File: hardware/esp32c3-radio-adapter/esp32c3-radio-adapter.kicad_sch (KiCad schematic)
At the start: 12 parts, among them J1 Conn_01x08, J2 Conn_01x08, J3 E07-M1101D_or_Ra-02, J4 Expansion

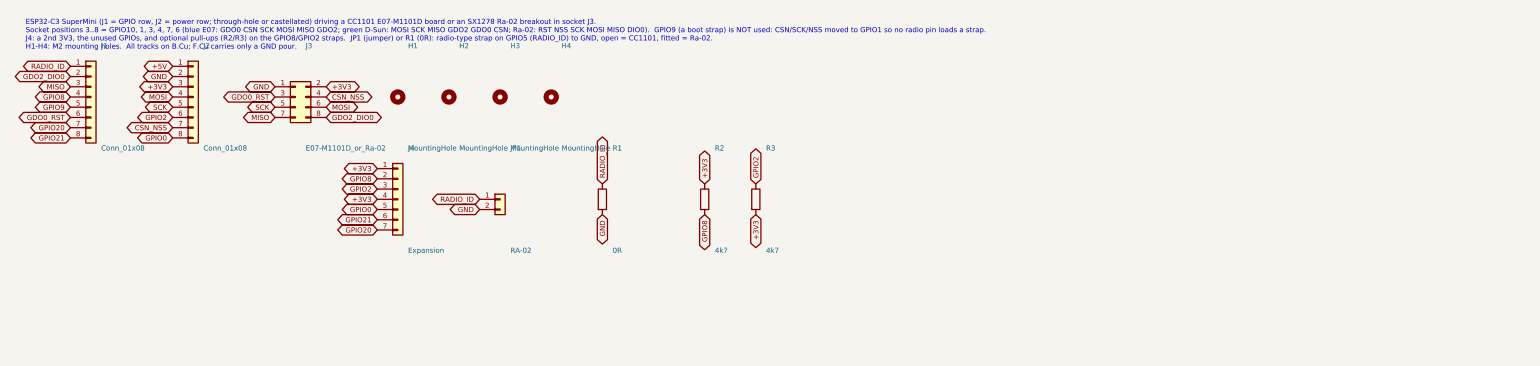
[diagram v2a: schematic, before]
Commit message: Socket adapter: J5, a fly-wire header for the SX1278's DIO2/DATA pin
In the SX1278's continuous mode the raw bitstream reaches the outside
world only on DIO2/DATA -- the FIFO and packet handler are inactive, and
Table 29 gives no other DIO that can carry it in Rx.  Packet mode can't
stand in: it only carries what the chip's packet handler can frame, which
is fine for the Fineoffset stations but useless for the OOK remotes this
node exists to hear and key.  DIO2 is the SX1278's GDO2, and the Ra-02
breakout leaves it on the module edge, unconnected.

Add J5, a 1x2 header carrying GPIO21 and GPIO20, so one wire from an
Ra-02's DIO2 pad reaches a GPIO.  GPIO20 is that pin; both stay on J4 as
well, so nothing is lost -- one net, brought out twice.

Placing it took the board from 36.5 to 38.0 mm tall.  A 2.54 mm header
body and both plugged-in boards all sit at board level, so the header has
to be clear of them in plan view, and the only such region is the band
between the SuperMini's body and the radio board's top edge.  At 36.5 mm
that band is 4.08 mm, which leaves 0.79 mm either side of the body;
1.5 mm more opens it to 5.58 mm and takes both margins to 1.54 mm.

Routing stays single-sided.  GPIO21 drops right of GPIO20, so it must
take the lane above J5's pads (25.29) and stubs down into pin 1; GPIO20
takes the lane below (27.8) and climbs the strip straight through its own
pad, pin 2.  That fixes which net is on which pin: GPIO20's strip lane
has to pass through a pad of its own net, and the gap right of pin 2 is
only 0.235 mm.  The four strip lanes shift left 0.45 mm to make room
(GPIO21 22.9, GPIO20 23.35) and 3V3/GND move out to 24.55/25.0, still
0.375 mm clear of the M2 holes.

GND is not on J5: reaching it would mean crossing the 3V3 strip lane, and
it isn't needed -- the boards already share GND through the socket.

The SX1278 module adapter is untouched; its pin allocation is to be
brought into line with this board separately.

Co-Authored-By: Claude Opus 5 (1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
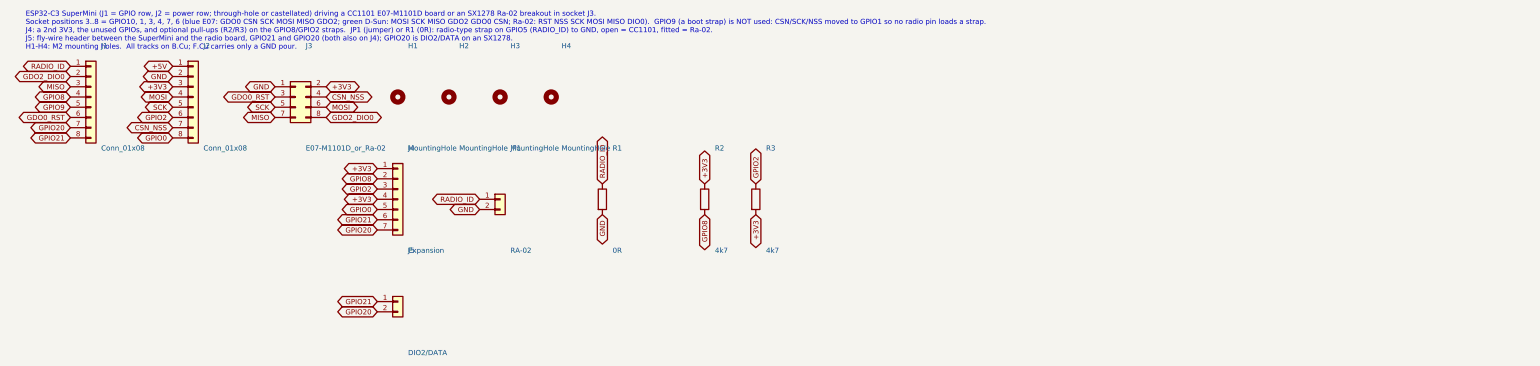
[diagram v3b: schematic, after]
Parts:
- added J5: DIO2/DATA, Adapter:PinHeader_1x02_P2.54mm_Vertical, symbol Connector_Generic:Conn_01x02
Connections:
- net GPIO20: now also J5.2 (Pin_2)
- net GPIO21: now also J5.1 (Pin_1)
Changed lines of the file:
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@@
+	)
+	(symbol
+		(lib_id "Connector_Generic:Conn_01x02")
+		(at 152.4 152.4 0)
+		(unit 1)
+		(exclude_from_sim no)
+		(in_bom yes)
+		(on_board yes)
+		(dnp no)
+		(fields_autoplaced yes)
+		(property "Reference" "J5"
+			(at 154.94 139.7 0)
+			(effects
+				(font
+					(size 1.27 1.27)
+				)
+				(justify left)
+			)
+		)
+		(property "Value" "DIO2/DATA"
+			(at 154.94 165.1 0)
+			(effects
+				(font
+					(size 1.27 1.27)
+				)
+				(justify left)
+			)
+		)
+		(property "Footprint" "Adapter:PinHeader_1x02_P2.54mm_Vertical"
+			(at 152.4 152.4 0)
+			(effects
+				(font
+					(size 1.27 1.27)
+				)
+				(hide yes)
+			)
+		)
+		(property "Datasheet" "~"
+			(at 152.4 152.4 0)
+			(effects
+				(font
+					(size 1.27 1.27)
+				)
+				(hide yes)
+			)
+		)
+		(property "Description" "Fly-wire header beside the socket: pin 2 (GPIO20) is the SX1278's DIO2/DATA raw-bitstream pin, pin 1 (GPIO21) a spare"
+			(at 152.4 152.4 0)
+			(effects
+				(font
+					(size 1.27 1.27)
+				)
+				(hide yes)
+			)
+		)
+		(pin "1"
+		)
+		(pin "2"
+		)
+		(instances
+			(project "esp32c3-radio-adapter"
+				(path "/b71943b6-a88f-5429-bfd6-fb1a52f93b27"
+					(reference "J5")
+					(unit 1)
+				)
+			)
+		)
+	)
+	(global_label "GPIO21"
+		(shape bidirectional)
+		(at 147.32 152.4 180)
+		(fields_autoplaced yes)
+		(effects
+			(font
+				(size 1.27 1.27)
+			)
+			(justify right)
+		)
+		(property "Intersheetrefs" "${INTERSHEET_REFS}"
+			(at 147.32 152.4 0)
+			(effects
+				(font
+					(size 1.27 1.27)
+				)
+				(justify right)
+				(hide yes)
+			)
+		)
+	)
+	(global_label "GPIO20"
+		(shape bidirectional)
+		(at 147.32 154.94 180)
+		(fields_autoplaced yes)
+		(effects
+			(font
+				(size 1.27 1.27)
+			)
+			(justify right)
+		)
+		(property "Intersheetrefs" "${INTERSHEET_REFS}"
+			(at 147.32 154.94 0)
+			(effects
+				(font
+					(size 1.27 1.27)
+				)
+				(justify right)
+				(hide yes)
+			)
+		)
 	)
 	(symbol
@@
 		)
 	)
-	(text "ESP32-C3 SuperMini (J1 = GPIO row, J2 = power row; through-hole or castellated) driving a CC1101 E07-M1101D board or an SX1278 Ra-02 breakout in socket J3.\nSocket positions 3..8 = GPIO10, 1, 3, 4, 7, 6 (blue E07: GDO0 CSN SCK MOSI MISO GDO2; green D-Sun: MOSI SCK MISO GDO2 GDO0 CSN; Ra-02: RST NSS SCK MOSI MISO DIO0).  GPIO9 (a boot strap) is NOT used: CSN/SCK/NSS moved to GPIO1 so no radio pin loads a strap.\nJ4: a 2nd 3V3, the unused GPIOs, and optional pull-ups (R2/R3) on the GPIO8/GPIO2 straps.  JP1 (jumper) or R1 (0R): radio-type strap on GPIO5 (RADIO_ID) to GND, open = CC1101, fitted = Ra-02.\nH1-H4: M2 mounting holes.  All tracks on B.Cu; F.Cu carries only a GND pour."
+	(text "ESP32-C3 SuperMini (J1 = GPIO row, J2 = power row; through-hole or castellated) driving a CC1101 E07-M1101D board or an SX1278 Ra-02 breakout in socket J3.\nSocket positions 3..8 = GPIO10, 1, 3, 4, 7, 6 (blue E07: GDO0 CSN SCK MOSI MISO GDO2; green D-Sun: MOSI SCK MISO GDO2 GDO0 CSN; Ra-02: RST NSS SCK MOSI MISO DIO0).  GPIO9 (a boot strap) is NOT used: CSN/SCK/NSS moved to GPIO1 so no radio pin loads a strap.\nJ4: a 2nd 3V3, the unused GPIOs, and optional pull-ups (R2/R3) on the GPIO8/GPIO2 straps.  JP1 (jumper) or R1 (0R): radio-type strap on GPIO5 (RADIO_ID) to GND, open = CC1101, fitted = Ra-02.\nJ5: fly-wire header between the SuperMini and the radio board, GPIO21 and GPIO20 (both also on J4); GPIO20 is DIO2/DATA on an SX1278.\nH1-H4: M2 mounting holes.  All tracks on B.Cu; F.Cu carries only a GND pour."
 		(exclude_from_sim no)
 		(at 60 90 0)

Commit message: Socket adapter: R4, a GPIO9 pull-up footprint, and clearer silkscreen
GPIO9 is the boot strap the socket no longer carries.  Give it the same
optional do-not-populate 4k7 pull-up to 3V3 the other two straps have.
Its pad is boxed in on the back copper (SCK passes left of it and drops
into the socket pin directly beneath, CSN passes right of it), so:
SCK steps one gap left as soon as it leaves its pad, J4 pins 3 and 4
swap so the second 3V3 sits left of GPIO2 like the first sits left of
GPIO8, and that 3V3 pin feeds down through the power row's GPIO3/GPIO2
gap into R4, whose other pad drops into GPIO9.  CSN keeps right of R4
until it is above the GPIO row's rings.  Still every track on B.Cu; DRC
clean.

Silkscreen: every SuperMini pin now has an inner label (NC, GND, 3V3,
J4, J4/J5, R4, JP1, DIO2 for the pins that carried none); the USB-C is
drawn as its outline instead of a word, solid on the front and dashed
on the back; every outline on the back is dashed; the "all tracks"
notes go, replaced by "parts this side" on the front.  Under the USB-C
outline the two columns' labels are shortened or split into two lines.

Co-Authored-By: Claude Opus 5 (1M context) <noreply@anthropic.com>
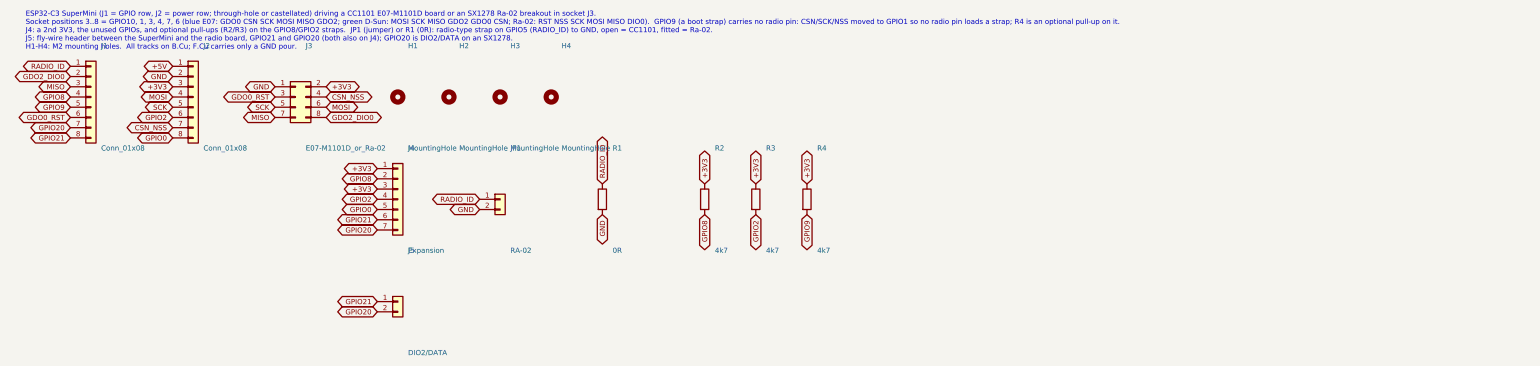
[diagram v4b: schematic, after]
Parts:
- added R4: 4k7, Adapter:R_0805_2012Metric_HandSolder_AlongY_Back, symbol Device:R
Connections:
- net +3V3: now also J4.3 (Pin_3), R3.1, R4.1; no longer J4.4 (Pin_4), R3.2
- net GPIO2: now also J4.4 (Pin_4), R3.2; no longer J4.3 (Pin_3), R3.1
- net GPIO9: now also R4.2
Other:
- note added: "ESP32-C3 SuperMini (J1 = GPIO row, J2 = power row; through-hole or castellated) driving a CC1101 E07-M1101D board or an SX1278 Ra-02 breakout in socket J3. Socket positions 3..8 = GPIO10, 1, 3, 4, 7, 6 (blue E07: GDO0 CSN SCK MOSI MISO GDO2; green D-Sun: MOSI SCK MISO GDO2 GDO0 CSN; Ra-02: RST NSS SCK MOSI MISO DIO0). GPIO9 (a boot strap) carries no radio pin: CSN/SCK/NSS moved to GPIO1 so no rad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"
- note removed: "ESP32-C3 SuperMini (J1 = GPIO row, J2 = power row; through-hole or castellated) driving a CC1101 E07-M1101D board or an SX1278 Ra-02 breakout in socket J3. Socket positions 3..8 = GPIO10, 1, 3, 4, 7, 6 (blue E07: GDO0 CSN SCK MOSI MISO GDO2; green D-Sun: MOSI SCK MISO GDO2 GDO0 CSN; Ra-02: RST NSS SCK MOSI MISO DIO0). GPIO9 (a boot strap) is NOT used: CSN/SCK/NSS moved to GPIO1 so no radio pin lo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"
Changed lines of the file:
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@@
+		)
+	)
+	(global_label "+3V3"
+		(shape bidirectional)
+		(at 147.32 124.46 180)
+		(fields_autoplaced yes)
+		(effects
+			(font
+				(size 1.27 1.27)
+			)
+			(justify right)
+		)
+		(property "Intersheetrefs" "${INTERSHEET_REFS}"
+			(at 147.32 124.46 0)
+			(effects
+				(font
+					(size 1.27 1.27)
+				)
+				(justify right)
+				(hide yes)
+			)
 		)
 	)
 	(global_label "GPIO2"
-		(shape bidirectional)
-		(at 147.32 124.46 180)
-		(fields_autoplaced yes)
-		(effects
-			(font
-				(size 1.27 1.27)
-			)
-			(justify right)
-		)
-		(property "Intersheetrefs" "${INTERSHEET_REFS}"
-			(at 147.32 124.46 0)
-			(effects
-				(font
-					(size 1.27 1.27)
-				)
-				(justify right)
-				(hide yes)
-			)
-		)
-	)
-	(global_label "+3V3"
 		(shape bidirectional)
 		(at 147.32 127 180)
@@
 		)
 	)
+	(global_label "+3V3"
+		(shape bidirectional)
+		(at 241.3 123.19 90)
+		(fields_autoplaced yes)
+		(effects
+			(font
+				(size 1.27 1.27)
+			)
+			(justify left)
+		)
+		(property "Intersheetrefs" "${INTERSHEET_REFS}"
+			(at 241.3 123.19 0)
+			(effects
+				(font
+					(size 1.27 1.27)
+				)
+				(justify left)
+				(hide yes)
+			)
+		)
+	)
 	(global_label "GPIO2"
 		(shape bidirectional)
-		(at 241.3 123.19 90)
+		(at 241.3 130.81 270)
+		(fields_autoplaced yes)
+		(effects
+			(font
+				(size 1.27 1.27)
+			)
+			(justify right)
+		)
+		(property "Intersheetrefs" "${INTERSHEET_REFS}"
+			(at 241.3 130.81 0)
+			(effects
+				(font
+					(size 1.27 1.27)
+				)
+				(justify right)
+				(hide yes)
+			)
+		)
+	)
+	(symbol
+		(lib_id "Device:R")
+		(at 254 127 0)
+		(unit 1)
+		(exclude_from_sim no)
+		(in_bom yes)
+		(on_board yes)
+		(dnp no)
+		(fields_autoplaced yes)
+		(property "Reference" "R4"
+			(at 256.54 114.3 0)
+			(effects
+				(font
+					(size 1.27 1.27)
+				)
+				(justify left)
+			)
+		)
+		(property "Value" "4k7"
+			(at 256.54 139.7 0)
+			(effects
+				(font
+					(size 1.27 1.27)
+				)
+				(justify left)
+			)
+		)
+		(property "Footprint" "Adapter:R_0805_2012Metric_HandSolder_AlongY_Back"
+			(at 254 127 0)
+			(effects
+				(font
+					(size 1.27 1.27)
+				)
+				(hide yes)
+			)
+		)
+		(property "Datasheet" "~"
+			(at 254 127 0)
+			(effects
+				(font
+					(size 1.27 1.27)
+				)
+				(hide yes)
+			)
+		)
+		(property "Description" "Optional pull-up: GPIO9 boot strap to 3V3 (DNP unless needed)"
+			(at 254 127 0)
+			(effects
+				(font
+					(size 1.27 1.27)
+				)
+				(hide yes)
+			)
+		)
+		(pin "1"
+		)
+		(pin "2"
+		)
+		(instances
+			(project "esp32c3-radio-adapter"
+				(path "/b71943b6-a88f-5429-bfd6-fb1a52f93b27"
+					(reference "R4")
+					(unit 1)
+				)
+			)
+		)
+	)
+	(global_label "+3V3"
+		(shape bidirectional)
+		(at 254 123.19 90)
 		(fields_autoplaced yes)
 		(effects
@@
 		)
 		(property "Intersheetrefs" "${INTERSHEET_REFS}"
-			(at 241.3 123.19 0)
-			(effects
-				(font
-					(size 1.27 1.27)
-				)
-				(justify left)
-				(hide yes)
-			)
-		)
-	)
-	(global_label "+3V3"
-		(shape bidirectional)
-		(at 241.3 130.81 270)
-		(fields_autoplaced yes)
-		(effects
-			(font
-				(size 1.27 1.27)
-			)
-			(justify right)
-		)
-		(property "Intersheetrefs" "${INTERSHEET_REFS}"
-			(at 241.3 130.81 0)
+			(at 254 123.19 0)
+			(effects
+				(font
+					(size 1.27 1.27)
+				)
+				(justify left)
+				(hide yes)
+			)
+		)
+	)
+	(global_label "GPIO9"
+		(shape bidirectional)
+		(at 254 130.81 270)
+		(fields_autoplaced yes)
+		(effects
+			(font
+				(size 1.27 1.27)
+			)
+			(justify right)
+		)
+		(property "Intersheetrefs" "${INTERSHEET_REFS}"
+			(at 254 130.81 0)
 			(effects
 				(font
@@
 		)
 	)
-	(text "ESP32-C3 SuperMini (J1 = GPIO row, J2 = power row; through-hole or castellated) driving a CC1101 E07-M1101D board or an SX1278 Ra-02 breakout in socket J3.\nSocket positions 3..8 = GPIO10, 1, 3, 4, 7, 6 (blue E07: GDO0 CSN SCK MOSI MISO GDO2; green D-Sun: MOSI SCK MISO GDO2 GDO0 CSN; Ra-02: RST NSS SCK MOSI MISO DIO0).  GPIO9 (a boot strap) is NOT used: CSN/SCK/NSS moved to GPIO1 so no radio pin loads a strap.\nJ4: a 2nd 3V3, the unused GPIOs, and optional pull-ups (R2/R3) on the GPIO8/GPIO2 straps.  JP1 (jumper) or R1 (0R): radio-type strap on GPIO5 (RADIO_ID) to GND, open = CC1101, fitted = Ra-02.\nJ5: fly-wire header between the SuperMini and the radio board, GPIO21 and GPIO20 (both also on J4); GPIO20 is DIO2/DATA on an SX1278.\nH1-H4: M2 mounting holes.  All tracks on B.Cu; F.Cu carries only a GND pour."
+	(text "ESP32-C3 SuperMini (J1 = GPIO row, J2 = power row; through-hole or castellated) driving a CC1101 E07-M1101D board or an SX1278 Ra-02 breakout in socket J3.\nSocket positions 3..8 = GPIO10, 1, 3, 4, 7, 6 (blue E07: GDO0 CSN SCK MOSI MISO GDO2; green D-Sun: MOSI SCK MISO GDO2 GDO0 CSN; Ra-02: RST NSS SCK MOSI MISO DIO0).  GPIO9 (a boot strap) carries no radio pin: CSN/SCK/NSS moved to GPIO1 so no radio pin loads a strap; R4 is an optional pull-up on it.\nJ4: a 2nd 3V3, the unused GPIOs, and optional pull-ups (R2/R3) on the GPIO8/GPIO2 straps.  JP1 (jumper) or R1 (0R): radio-type strap on GPIO5 (RADIO_ID) to GND, open = CC1101, fitted = Ra-02.\nJ5: fly-wire header between the SuperMini and the radio board, GPIO21 and GPIO20 (both also on J4); GPIO20 is DIO2/DATA on an SX1278.\nH1-H4: M2 mounting holes.  All tracks on B.Cu; F.Cu carries only a GND pour."
 		(exclude_from_sim no)
 		(at 60 90 0)
